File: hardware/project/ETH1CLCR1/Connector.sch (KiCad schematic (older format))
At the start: 8 parts, among them J1201 C64AC, K1201 HE3621A0510, K1202 HE3621A0510, K1203 HE3621A0510, K1204 HE3621A0510, K1205 HE3621A0510, K1206 HE3621A0510, U1201 ULN2003A

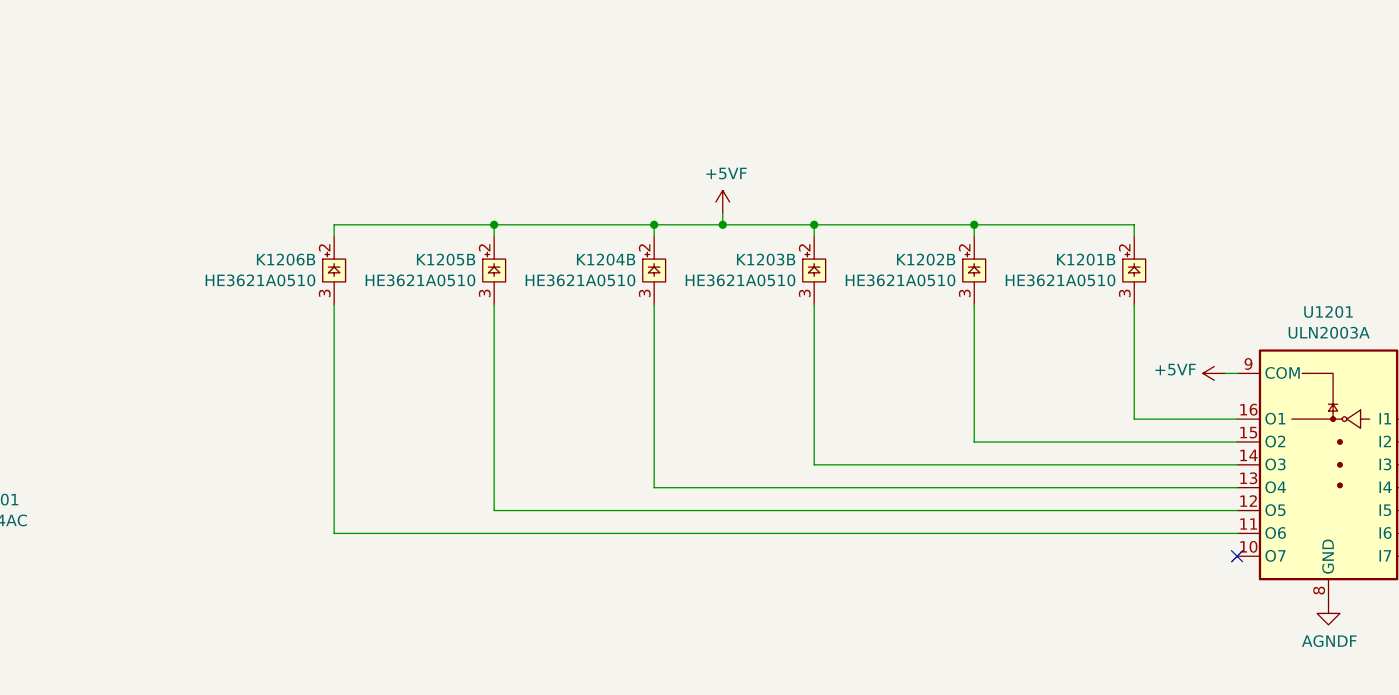
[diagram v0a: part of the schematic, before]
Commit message: Checked the schematics. Created BOM.
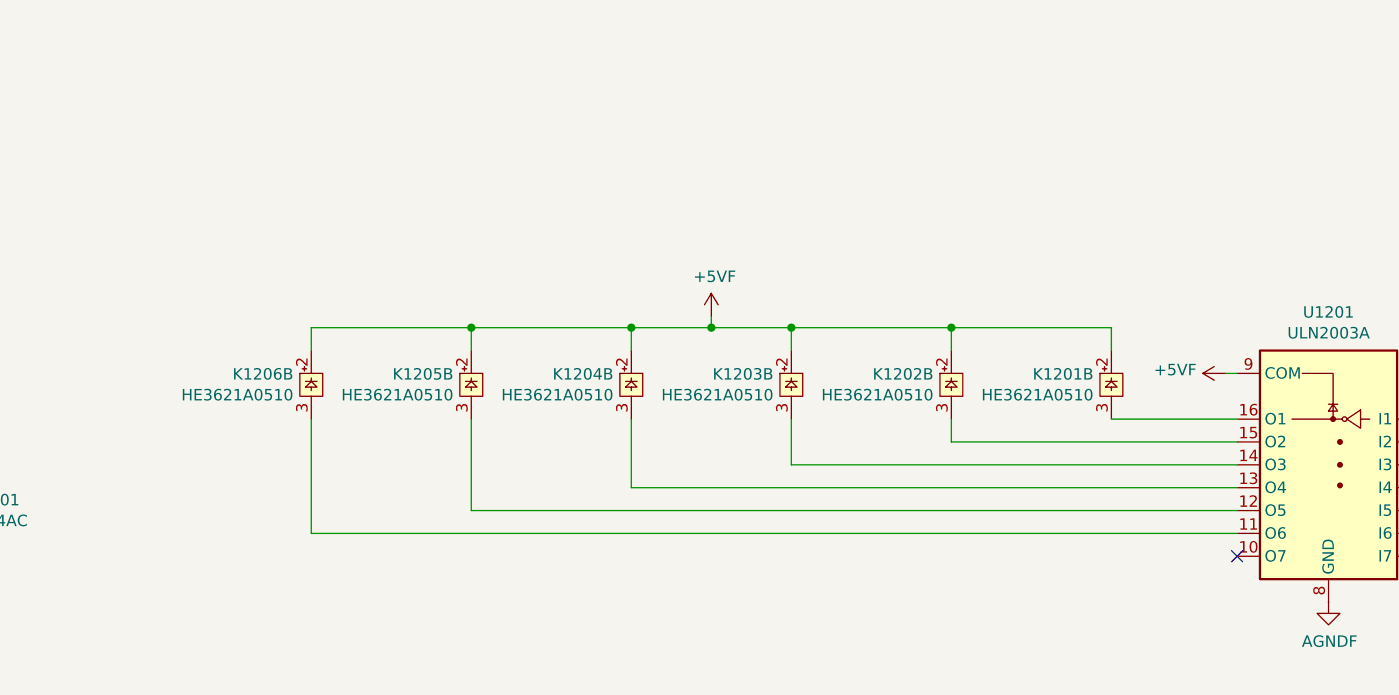
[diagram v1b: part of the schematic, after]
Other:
- moved on the sheet: K1201B, K1202B, K1203B, K1204B, K1205B, K1206B
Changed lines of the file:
@@
 encoding utf-8
 Sheet 12 15
-Title ""
-Date ""
-Rev ""
+Title "Connector"
+Date "2020-01-19"
+Rev "1.0"
 Comp ""
-Comment1 ""
+Comment1 "Verification done. "
 Comment2 ""
 Comment3 ""
@@
 NoConn ~ 9150 4250
 Wire Wire Line
-	5200 4150 5200 3150
-Wire Wire Line
-	9150 4150 5200 4150
-Wire Wire Line
-	5900 4050 5900 3150
-Wire Wire Line
-	9150 4050 5900 4050
-Wire Wire Line
-	6600 3950 6600 3150
-Wire Wire Line
-	9150 3950 6600 3950
-Wire Wire Line
-	7300 3850 7300 3150
-Wire Wire Line
-	9150 3850 7300 3850
-Wire Wire Line
-	8000 3750 8000 3150
-Wire Wire Line
-	9150 3750 8000 3750
-Wire Wire Line
-	8700 3650 8700 3150
-Wire Wire Line
-	9150 3650 8700 3650
-Wire Wire Line
-	6900 2800 6600 2800
-Connection ~ 6900 2800
-Wire Wire Line
-	6900 2750 6900 2800
+	5100 4150 5100 3650
+Wire Wire Line
+	9150 4150 5100 4150
+Wire Wire Line
+	5800 4050 5800 3650
+Wire Wire Line
+	9150 4050 5800 4050
+Wire Wire Line
+	6500 3950 6500 3650
+Wire Wire Line
+	9150 3950 6500 3950
+Wire Wire Line
+	7200 3850 7200 3650
+Wire Wire Line
+	9150 3850 7200 3850
+Wire Wire Line
+	7900 3750 7900 3650
+Wire Wire Line
+	9150 3750 7900 3750
+Wire Wire Line
+	9150 3650 8600 3650
+Wire Wire Line
+	6850 3250 6500 3250
+Connection ~ 6850 3250
+Wire Wire Line
+	6850 3200 6850 3250
 $Comp
 L ETH1CLCR1:+5VF #PWR01207
 U 1 1 5E5FEFEE
-P 6900 2750
-F 0 "#PWR01207" H 6900 2600 50  0001 C CNN
-F 1 "+5VF" H 6915 2923 50  0000 C CNN
-F 2 "" H 6900 2750 50  0001 C CNN
-F 3 "" H 6900 2750 50  0001 C CNN
-	1    6900 2750
+P 6850 3200
+F 0 "#PWR01207" H 6850 3050 50  0001 C CNN
+F 1 "+5VF" H 6865 3373 50  0000 C CNN
+F 2 "" H 6850 3200 50  0001 C CNN
+F 3 "" H 6850 3200 50  0001 C CNN
+	1    6850 3200
 	1    0    0    -1
 $EndComp
 Wire Wire Line
-	8000 2800 7300 2800
-Connection ~ 8000 2800
-Wire Wire Line
-	8000 2850 8000 2800
-Wire Wire Line
-	7300 2800 6900 2800
-Connection ~ 7300 2800
-Wire Wire Line
-	7300 2850 7300 2800
-Wire Wire Line
-	6600 2800 5900 2800
-Connection ~ 6600 2800
-Wire Wire Line
-	6600 2850 6600 2800
-Wire Wire Line
-	5900 2800 5200 2800
-Connection ~ 5900 2800
-Wire Wire Line
-	5900 2850 5900 2800
-Wire Wire Line
-	5200 2800 5200 2850
-Wire Wire Line
-	8700 2800 8000 2800
-Wire Wire Line
-	8700 2850 8700 2800
+	7900 3250 7200 3250
+Connection ~ 7900 3250
+Wire Wire Line
+	7900 3350 7900 3250
+Wire Wire Line
+	7200 3250 6850 3250
+Connection ~ 7200 3250
+Wire Wire Line
+	7200 3350 7200 3250
+Wire Wire Line
+	6500 3250 5800 3250
+Connection ~ 6500 3250
+Wire Wire Line
+	6500 3350 6500 3250
+Wire Wire Line
+	5800 3250 5100 3250
+Connection ~ 5800 3250
+Wire Wire Line
+	5800 3350 5800 3250
+Wire Wire Line
+	5100 3250 5100 3350
+Wire Wire Line
+	8600 3250 7900 3250
+Wire Wire Line
+	8600 3350 8600 3250
 Wire Wire Line
 	9100 3450 9150 3450
@@
 L ETH1CLCR1:HE3621A0510 K1205
 U 2 1 5E1D6511
-P 5900 3000
-F 0 "K1205" H 5978 3046 50  0000 L CNN
-F 1 "HE3621A0510" H 5978 2955 50  0000 L CNN
-F 2 "ETH1CLCR1:HE360_x-5050462-8" H 6150 2950 50  0001 C CNN
-F 3 "" H 6150 2950 50  0001 C CNN
-	2    5900 3000
+P 5800 3500
+F 0 "K1205" H 5878 3546 50  0000 L CNN
+F 1 "HE3621A0510" H 5878 3455 50  0000 L CNN
+F 2 "ETH1CLCR1:HE360_x-5050462-8" H 6050 3450 50  0001 C CNN
+F 3 "" H 6050 3450 50  0001 C CNN
+	2    5800 3500
 	-1   0    0    -1
 $EndComp
@@
 L ETH1CLCR1:HE3621A0510 K1204
 U 2 1 5E1D1D0B
-P 6600 3000
-F 0 "K1204" H 6678 3046 50  0000 L CNN
-F 1 "HE3621A0510" H 6678 2955 50  0000 L CNN
-F 2 "ETH1CLCR1:HE360_x-5050462-8" H 6850 2950 50  0001 C CNN
-F 3 "" H 6850 2950 50  0001 C CNN
-	2    6600 3000
+P 6500 3500
+F 0 "K1204" H 6578 3546 50  0000 L CNN
+F 1 "HE3621A0510" H 6578 3455 50  0000 L CNN
+F 2 "ETH1CLCR1:HE360_x-5050462-8" H 6750 3450 50  0001 C CNN
+F 3 "" H 6750 3450 50  0001 C CNN
+	2    6500 3500
 	-1   0    0    -1
 $EndComp
@@
 L ETH1CLCR1:HE3621A0510 K1203
 U 2 1 5E1CE0D5
-P 7300 3000
-F 0 "K1203" H 7378 3046 50  0000 L CNN
-F 1 "HE3621A0510" H 7378 2955 50  0000 L CNN
-F 2 "ETH1CLCR1:HE360_x-5050462-8" H 7550 2950 50  0001 C CNN
-F 3 "" H 7550 2950 50  0001 C CNN
-	2    7300 3000
+P 7200 3500
+F 0 "K1203" H 7278 3546 50  0000 L CNN
+F 1 "HE3621A0510" H 7278 3455 50  0000 L CNN
+F 2 "ETH1CLCR1:HE360_x-5050462-8" H 7450 3450 50  0001 C CNN
+F 3 "" H 7450 3450 50  0001 C CNN
+	2    7200 3500
 	-1   0    0    -1
 $EndComp
@@
 L ETH1CLCR1:HE3621A0510 K1202
 U 2 1 5E1C97AD
-P 8000 3000
-F 0 "K1202" H 8078 3046 50  0000 L CNN
-F 1 "HE3621A0510" H 8078 2955 50  0000 L CNN
-F 2 "ETH1CLCR1:HE360_x-5050462-8" H 8250 2950 50  0001 C CNN
-F 3 "" H 8250 2950 50  0001 C CNN
-	2    8000 3000
+P 7900 3500
+F 0 "K1202" H 7978 3546 50  0000 L CNN
+F 1 "HE3621A0510" H 7978 3455 50  0000 L CNN
+F 2 "ETH1CLCR1:HE360_x-5050462-8" H 8150 3450 50  0001 C CNN
+F 3 "" H 8150 3450 50  0001 C CNN
+	2    7900 3500
 	-1   0    0    -1
 $EndComp
@@
 L ETH1CLCR1:HE3621A0510 K1206
 U 2 1 5E1C5D99
-P 5200 3000
-F 0 "K1206" H 5278 3046 50  0000 L CNN
-F 1 "HE3621A0510" H 5278 2955 50  0000 L CNN
-F 2 "ETH1CLCR1:HE360_x-5050462-8" H 5450 2950 50  0001 C CNN
-F 3 "" H 5450 2950 50  0001 C CNN
-	2    5200 3000
+P 5100 3500
+F 0 "K1206" H 5178 3546 50  0000 L CNN
+F 1 "HE3621A0510" H 5178 3455 50  0000 L CNN
+F 2 "ETH1CLCR1:HE360_x-5050462-8" H 5350 3450 50  0001 C CNN
+F 3 "" H 5350 3450 50  0001 C CNN
+	2    5100 3500
 	-1   0    0    -1
 $EndComp
@@
 L ETH1CLCR1:HE3621A0510 K1201
 U 2 1 5E1C1048
-P 8700 3000
-F 0 "K1201" H 8778 3046 50  0000 L CNN
-F 1 "HE3621A0510" H 8778 2955 50  0000 L CNN
-F 2 "ETH1CLCR1:HE360_x-5050462-8" H 8950 2950 50  0001 C CNN
-F 3 "" H 8950 2950 50  0001 C CNN
-	2    8700 3000
-	-1   0    0    -1
-$EndComp
+P 8600 3500
+F 0 "K1201" H 8678 3546 50  0000 L CNN
+F 1 "HE3621A0510" H 8678 3455 50  0000 L CNN
+F 2 "ETH1CLCR1:HE360_x-5050462-8" H 8850 3450 50  0001 C CNN
+F 3 "" H 8850 3450 50  0001 C CNN
+	2    8600 3500
+	-1   0    0    -1
+$EndComp

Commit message: PCB layout
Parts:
- added C1201: 100n, Capacitor_SMD:C_0603_1608Metric_Pad1.05x0.95mm_HandSolder, symbol Device:C
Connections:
- net +5VF: now also C1201.1
- net AGNDF: now also C1201.2
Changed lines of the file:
@@
 Text HLabel 10000 3650 2    50   Input ~ 0
 CXN_REL1
+$Comp
+L Device:C C?
+U 1 1 5E417543
+P 10800 3900
+AR Path="/5DEA9498/5E417543" Ref="C?"  Part="1"
+AR Path="/5DEACCC1/5E417543" Ref="C1201"  Part="1"
+F 0 "C1201" H 10915 3946 50  0000 L CNN
+F 1 "100n" H 10915 3855 50  0000 L CNN
+F 2 "Capacitor_SMD:C_0603_1608Metric_Pad1.05x0.95mm_HandSolder" H 10838 3750 50  0001 C CNN
+F 3 "~" H 10800 3900 50  0001 C CNN
+	1    10800 3900
+	1    0    0    -1
+$EndComp
+Wire Wire Line
+	10800 4150 10800 4050
+Wire Wire Line
+	10800 3750 10800 3650
+$Comp
+L ETH1CLCR1:AGNDF #PWR01211
+U 1 1 5E41A57F
+P 10800 4150
+F 0 "#PWR01211" H 10800 3900 50  0001 C CNN
+F 1 "AGNDF" H 10805 3977 50  0000 C CNN
+F 2 "" H 10800 4150 50  0001 C CNN
+F 3 "" H 10800 4150 50  0001 C CNN
+	1    10800 4150
+	1    0    0    -1
+$EndComp
+$Comp
+L ETH1CLCR1:+5VF #PWR01210
+U 1 1 5E41E46C
+P 10800 3650
+F 0 "#PWR01210" H 10800 3500 50  0001 C CNN
+F 1 "+5VF" H 10815 3823 50  0000 C CNN
+F 2 "" H 10800 3650 50  0001 C CNN
+F 3 "" H 10800 3650 50  0001 C CNN
+	1    10800 3650
+	1    0    0    -1
+$EndComp
 $EndSCHEMATC

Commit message: PCB layout
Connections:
- net CXN_REL1: now also U1201.6 (I6); no longer U1201.1 (I1)
- net CXN_REL2: now also U1201.5 (I5); no longer U1201.2 (I2)
- net CXN_REL3: now also U1201.4 (I4); no longer U1201.3 (I3)
- net CXN_REL4: now also U1201.3 (I3); no longer U1201.4 (I4)
- net CXN_REL5: now also U1201.2 (I2); no longer U1201.5 (I5)
- net CXN_REL6: now also U1201.1 (I1); no longer U1201.6 (I6)
- net at K1201.3: now also U1201.11 (O6); no longer U1201.16 (O1)
- net at K1206.3: now also U1201.16 (O1); no longer U1201.11 (O6)
- net at K1202.3: now also U1201.12 (O5); no longer U1201.15 (O2)
- net at K1203.3: now also U1201.13 (O4); no longer U1201.14 (O3)
- net at K1204.3: now also U1201.14 (O3); no longer U1201.13 (O4)
- net at K1205.3: now also U1201.15 (O2); no longer U1201.12 (O5)
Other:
- moved on the sheet: K1201B, K1202B, K1203B, K1204B, K1205B, K1206B
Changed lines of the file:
@@
 $EndComp
 Wire Wire Line
-	10000 3650 9950 3650
-Wire Wire Line
-	9950 3750 10000 3750
-Wire Wire Line
-	10000 3850 9950 3850
-Wire Wire Line
-	9950 3950 10000 3950
-Wire Wire Line
-	10000 4050 9950 4050
-Wire Wire Line
-	9950 4150 10000 4150
+	10000 4150 9950 4150
+Wire Wire Line
+	9950 4050 10000 4050
+Wire Wire Line
+	10000 3950 9950 3950
+Wire Wire Line
+	9950 3850 10000 3850
+Wire Wire Line
+	10000 3750 9950 3750
+Wire Wire Line
+	9950 3650 10000 3650
 NoConn ~ 9950 4250
 NoConn ~ 9150 4250
 Wire Wire Line
-	5100 4150 5100 3650
-Wire Wire Line
-	9150 4150 5100 4150
-Wire Wire Line
-	5800 4050 5800 3650
-Wire Wire Line
-	9150 4050 5800 4050
-Wire Wire Line
-	6500 3950 6500 3650
-Wire Wire Line
-	9150 3950 6500 3950
-Wire Wire Line
-	7200 3850 7200 3650
-Wire Wire Line
-	9150 3850 7200 3850
-Wire Wire Line
-	7900 3750 7900 3650
-Wire Wire Line
-	9150 3750 7900 3750
-Wire Wire Line
-	9150 3650 8600 3650
-Wire Wire Line
-	6850 3250 6500 3250
-Connection ~ 6850 3250
-Wire Wire Line
-	6850 3200 6850 3250
+	4500 4150 4500 3650
+Wire Wire Line
+	9150 4150 4500 4150
+Wire Wire Line
+	5200 4050 5200 3650
+Wire Wire Line
+	9150 4050 5200 4050
+Wire Wire Line
+	5900 3950 5900 3650
+Wire Wire Line
+	9150 3950 5900 3950
+Wire Wire Line
+	6600 3850 6600 3650
+Wire Wire Line
+	9150 3850 6600 3850
+Wire Wire Line
+	7300 3750 7300 3650
+Wire Wire Line
+	9150 3750 7300 3750
+Wire Wire Line
+	9150 3650 8000 3650
+Wire Wire Line
+	6250 3250 5900 3250
+Connection ~ 6250 3250
+Wire Wire Line
+	6250 3200 6250 3250
 $Comp
 L ETH1CLCR1:+5VF #PWR01207
 U 1 1 5E5FEFEE
-P 6850 3200
-F 0 "#PWR01207" H 6850 3050 50  0001 C CNN
-F 1 "+5VF" H 6865 3373 50  0000 C CNN
-F 2 "" H 6850 3200 50  0001 C CNN
-F 3 "" H 6850 3200 50  0001 C CNN
-	1    6850 3200
-	1    0    0    -1
-$EndComp
-Wire Wire Line
-	7900 3250 7200 3250
-Connection ~ 7900 3250
-Wire Wire Line
-	7900 3350 7900 3250
-Wire Wire Line
-	7200 3250 6850 3250
-Connection ~ 7200 3250
-Wire Wire Line
-	7200 3350 7200 3250
-Wire Wire Line
-	6500 3250 5800 3250
-Connection ~ 6500 3250
-Wire Wire Line
-	6500 3350 6500 3250
-Wire Wire Line
-	5800 3250 5100 3250
-Connection ~ 5800 3250
-Wire Wire Line
-	5800 3350 5800 3250
-Wire Wire Line
-	5100 3250 5100 3350
-Wire Wire Line
-	8600 3250 7900 3250
-Wire Wire Line
-	8600 3350 8600 3250
+P 6250 3200
+F 0 "#PWR01207" H 6250 3050 50  0001 C CNN
+F 1 "+5VF" H 6265 3373 50  0000 C CNN
+F 2 "" H 6250 3200 50  0001 C CNN
+F 3 "" H 6250 3200 50  0001 C CNN
+	1    6250 3200
+	1    0    0    -1
+$EndComp
+Wire Wire Line
+	7300 3250 6600 3250
+Connection ~ 7300 3250
+Wire Wire Line
+	6600 3250 6250 3250
+Connection ~ 6600 3250
+Wire Wire Line
+	5900 3250 5200 3250
+Connection ~ 5900 3250
+Wire Wire Line
+	5200 3250 4500 3250
+Connection ~ 5200 3250
+Wire Wire Line
+	8000 3250 7300 3250
 Wire Wire Line
 	9100 3450 9150 3450
@@
 	-1   0    0    -1
 $EndComp
+Text HLabel 10000 3650 2    50   Input ~ 0
+CXN_REL6
+Text HLabel 10000 3750 2    50   Input ~ 0
+CXN_REL5
+Text HLabel 10000 3850 2    50   Input ~ 0
+CXN_REL4
+Text HLabel 10000 3950 2    50   Input ~ 0
+CXN_REL3
+Text HLabel 10000 4050 2    50   Input ~ 0
+CXN_REL2
 Text HLabel 10000 4150 2    50   Input ~ 0
-CXN_REL6
-Text HLabel 10000 4050 2    50   Input ~ 0
-CXN_REL5
-Text HLabel 10000 3950 2    50   Input ~ 0
-CXN_REL4
-$Comp
-L ETH1CLCR1:HE3621A0510 K1205
-U 2 1 5E1D6511
-P 5800 3500
-F 0 "K1205" H 5878 3546 50  0000 L CNN
-F 1 "HE3621A0510" H 5878 3455 50  0000 L CNN
-F 2 "ETH1CLCR1:HE360_x-5050462-8" H 6050 3450 50  0001 C CNN
-F 3 "" H 6050 3450 50  0001 C CNN
-	2    5800 3500
-	-1   0    0    -1
-$EndComp
-$Comp
-L ETH1CLCR1:HE3621A0510 K1204
-U 2 1 5E1D1D0B
-P 6500 3500
-F 0 "K1204" H 6578 3546 50  0000 L CNN
-F 1 "HE3621A0510" H 6578 3455 50  0000 L CNN
-F 2 "ETH1CLCR1:HE360_x-5050462-8" H 6750 3450 50  0001 C CNN
-F 3 "" H 6750 3450 50  0001 C CNN
-	2    6500 3500
-	-1   0    0    -1
-$EndComp
-$Comp
-L ETH1CLCR1:HE3621A0510 K1203
-U 2 1 5E1CE0D5
-P 7200 3500
-F 0 "K1203" H 7278 3546 50  0000 L CNN
-F 1 "HE3621A0510" H 7278 3455 50  0000 L CNN
-F 2 "ETH1CLCR1:HE360_x-5050462-8" H 7450 3450 50  0001 C CNN
-F 3 "" H 7450 3450 50  0001 C CNN
-	2    7200 3500
-	-1   0    0    -1
-$EndComp
-$Comp
-L ETH1CLCR1:HE3621A0510 K1202
-U 2 1 5E1C97AD
-P 7900 3500
-F 0 "K1202" H 7978 3546 50  0000 L CNN
-F 1 "HE3621A0510" H 7978 3455 50  0000 L CNN
-F 2 "ETH1CLCR1:HE360_x-5050462-8" H 8150 3450 50  0001 C CNN
-F 3 "" H 8150 3450 50  0001 C CNN
-	2    7900 3500
-	-1   0    0    -1
-$EndComp
-$Comp
-L ETH1CLCR1:HE3621A0510 K1206
-U 2 1 5E1C5D99
-P 5100 3500
-F 0 "K1206" H 5178 3546 50  0000 L CNN
-F 1 "HE3621A0510" H 5178 3455 50  0000 L CNN
-F 2 "ETH1CLCR1:HE360_x-5050462-8" H 5350 3450 50  0001 C CNN
-F 3 "" H 5350 3450 50  0001 C CNN
-	2    5100 3500
-	-1   0    0    -1
-$EndComp
-$Comp
-L ETH1CLCR1:HE3621A0510 K1201
-U 2 1 5E1C1048
-P 8600 3500
-F 0 "K1201" H 8678 3546 50  0000 L CNN
-F 1 "HE3621A0510" H 8678 3455 50  0000 L CNN
-F 2 "ETH1CLCR1:HE360_x-5050462-8" H 8850 3450 50  0001 C CNN
-F 3 "" H 8850 3450 50  0001 C CNN
-	2    8600 3500
-	-1   0    0    -1
-$EndComp
-Text HLabel 10000 3850 2    50   Input ~ 0
-CXN_REL3
-Text HLabel 10000 3750 2    50   Input ~ 0
-CXN_REL2
-Text HLabel 10000 3650 2    50   Input ~ 0
 CXN_REL1
 $Comp
@@
 	1    0    0    -1
 $EndComp
+$Comp
+L ETH1CLCR1:HE3621A0510 K1201
+U 2 1 5E1C1048
+P 4500 3500
+F 0 "K1201" H 4578 3546 50  0000 L CNN
+F 1 "HE3621A0510" H 4578 3455 50  0000 L CNN
+F 2 "ETH1CLCR1:HE360_x-5050462-8" H 4750 3450 50  0001 C CNN
+F 3 "" H 4750 3450 50  0001 C CNN
+	2    4500 3500
+	1    0    0    -1
+$EndComp
+$Comp
+L ETH1CLCR1:HE3621A0510 K1206
+U 2 1 5E1C5D99
+P 8000 3500
+F 0 "K1206" H 8078 3546 50  0000 L CNN
+F 1 "HE3621A0510" H 8078 3455 50  0000 L CNN
+F 2 "ETH1CLCR1:HE360_x-5050462-8" H 8250 3450 50  0001 C CNN
+F 3 "" H 8250 3450 50  0001 C CNN
+	2    8000 3500
+	1    0    0    -1
+$EndComp
+$Comp
+L ETH1CLCR1:HE3621A0510 K1202
+U 2 1 5E1C97AD
+P 5200 3500
+F 0 "K1202" H 5278 3546 50  0000 L CNN
+F 1 "HE3621A0510" H 5278 3455 50  0000 L CNN
+F 2 "ETH1CLCR1:HE360_x-5050462-8" H 5450 3450 50  0001 C CNN
+F 3 "" H 5450 3450 50  0001 C CNN
+	2    5200 3500
+	1    0    0    -1
+$EndComp
+$Comp
+L ETH1CLCR1:HE3621A0510 K1203
+U 2 1 5E1CE0D5
+P 5900 3500
+F 0 "K1203" H 5978 3546 50  0000 L CNN
+F 1 "HE3621A0510" H 5978 3455 50  0000 L CNN
+F 2 "ETH1CLCR1:HE360_x-5050462-8" H 6150 3450 50  0001 C CNN
+F 3 "" H 6150 3450 50  0001 C CNN
+	2    5900 3500
+	1    0    0    -1
+$EndComp
+$Comp
+L ETH1CLCR1:HE3621A0510 K1204
+U 2 1 5E1D1D0B
+P 6600 3500
+F 0 "K1204" H 6678 3546 50  0000 L CNN
+F 1 "HE3621A0510" H 6678 3455 50  0000 L CNN
+F 2 "ETH1CLCR1:HE360_x-5050462-8" H 6850 3450 50  0001 C CNN
+F 3 "" H 6850 3450 50  0001 C CNN
+	2    6600 3500
+	1    0    0    -1
+$EndComp
+$Comp
+L ETH1CLCR1:HE3621A0510 K1205
+U 2 1 5E1D6511
+P 7300 3500
+F 0 "K1205" H 7378 3546 50  0000 L CNN
+F 1 "HE3621A0510" H 7378 3455 50  0000 L CNN
+F 2 "ETH1CLCR1:HE360_x-5050462-8" H 7550 3450 50  0001 C CNN
+F 3 "" H 7550 3450 50  0001 C CNN
+	2    7300 3500
+	1    0    0    -1
+$EndComp
+Wire Wire Line
+	8000 3350 8000 3250
+Wire Wire Line
+	4500 3250 4500 3350
+Wire Wire Line
+	5200 3350 5200 3250
+Wire Wire Line
+	5900 3350 5900 3250
+Wire Wire Line
+	6600 3350 6600 3250
+Wire Wire Line
+	7300 3350 7300 3250
 $EndSCHEMATC

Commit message: PCB layout
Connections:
- net I: now reaches J1201.A10 (10A)
- net I: now also J1201.C10 (10C)
- net K: now reaches J1201.A11 (11A)
- net K: now also J1201.C11 (11C)
- net L: now reaches J1201.A12 (12A)
- net L: now also J1201.C12 (12C)
- net M: now reaches J1201.A13 (13A)
- net M: now also J1201.C13 (13C)
- net G: now reaches J1201.A8 (8A)
- net G: now also J1201.C8 (8C)
- net H: now reaches J1201.A9 (9A)
- net H: now also J1201.C9 (9C)
- no-connect marks 36 -> 24
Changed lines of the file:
@@
 NoConn ~ 3150 3600
 NoConn ~ 3150 3500
-NoConn ~ 3150 3400
-NoConn ~ 3150 3300
-NoConn ~ 3150 3200
-NoConn ~ 3150 3100
-NoConn ~ 3150 3000
-NoConn ~ 3150 2900
-NoConn ~ 3150 2800
-NoConn ~ 3150 2700
-NoConn ~ 3150 2600
-NoConn ~ 3150 2500
-NoConn ~ 3150 2400
-NoConn ~ 3150 2300
 NoConn ~ 3150 4600
 NoConn ~ 3150 4500
@@
 Wire Wire Line
 	3150 7200 3100 7200
-$Comp
-L Connector:C64AC J1201
-U 1 1 5DE8758D
-P 3450 4100
-F 0 "J1201" H 3630 4196 50  0000 L CNN
-F 1 "C64AC" H 3630 4105 50  0000 L CNN
-F 2 "ETH1CLCR1:Socket_DIN41612-CaseC1-AC-Male-64Pin-2rows" H 3450 4150 50  0001 C CNN
-F 3 " ~" H 3450 4150 50  0001 C CNN
-	1    3450 4100
-	1    0    0    -1
-$EndComp
 $Comp
 L ETH1CLCR1:AGNDF #PWR01209
@@
 Wire Wire Line
 	7300 3350 7300 3250
+Wire Wire Line
+	3150 2300 3100 2300
+Wire Wire Line
+	3100 2300 3100 2350
+Wire Wire Line
+	3100 2400 3150 2400
+Wire Wire Line
+	3100 2350 2900 2350
+Connection ~ 3100 2350
+Wire Wire Line
+	3100 2350 3100 2400
+Text Label 2900 2350 0    50   ~ 0
+G
+Wire Wire Line
+	3150 2500 3100 2500
+Wire Wire Line
+	3100 2500 3100 2550
+Wire Wire Line
+	3100 2600 3150 2600
+Wire Wire Line
+	3150 2700 3100 2700
+Wire Wire Line
+	3100 2700 3100 2750
+Wire Wire Line
+	3100 2800 3150 2800
+Wire Wire Line
+	2900 2550 3100 2550
+Connection ~ 3100 2550
+Wire Wire Line
+	3100 2550 3100 2600
+Text Label 2900 2550 0    50   ~ 0
+H
+Wire Wire Line
+	2900 2750 3100 2750
+Connection ~ 3100 2750
+Wire Wire Line
+	3100 2750 3100 2800
+Text Label 2900 2750 0    50   ~ 0
+I
+Wire Wire Line
+	3150 2900 3100 2900
+Wire Wire Line
+	3100 2900 3100 2950
+Wire Wire Line
+	3100 3000 3150 3000
+Wire Wire Line
+	3100 2950 2900 2950
+Connection ~ 3100 2950
+Wire Wire Line
+	3100 2950 3100 3000
+Text Label 2900 2950 0    50   ~ 0
+K
+$Comp
+L Connector:C64AC J1201
+U 1 1 5DE8758D
+P 3450 4100
+F 0 "J1201" H 3630 4196 50  0000 L CNN
+F 1 "C64AC" H 3630 4105 50  0000 L CNN
+F 2 "ETH1CLCR1:Socket_DIN41612-CaseC1-AC-Male-64Pin-2rows" H 3450 4150 50  0001 C CNN
+F 3 " ~" H 3450 4150 50  0001 C CNN
+	1    3450 4100
+	1    0    0    -1
+$EndComp
+Wire Wire Line
+	3150 3100 3100 3100
+Wire Wire Line
+	3100 3100 3100 3150
+Wire Wire Line
+	3100 3200 3150 3200
+Wire Wire Line
+	3100 3150 2900 3150
+Connection ~ 3100 3150
+Wire Wire Line
+	3100 3150 3100 3200
+Text Label 2900 3150 0    50   ~ 0
+L
+Wire Wire Line
+	3150 3400 3100 3400
+Wire Wire Line
+	3100 3400 3100 3350
+Wire Wire Line
+	3100 3300 3150 3300
+Wire Wire Line
+	3100 3350 2900 3350
+Connection ~ 3100 3350
+Wire Wire Line
+	3100 3350 3100 3300
+Text Label 2900 3350 0    50   ~ 0
+M
 $EndSCHEMATC
